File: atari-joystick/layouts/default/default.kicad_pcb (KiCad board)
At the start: 2 copper layers, 31.2 x 30 mm, 15 parts

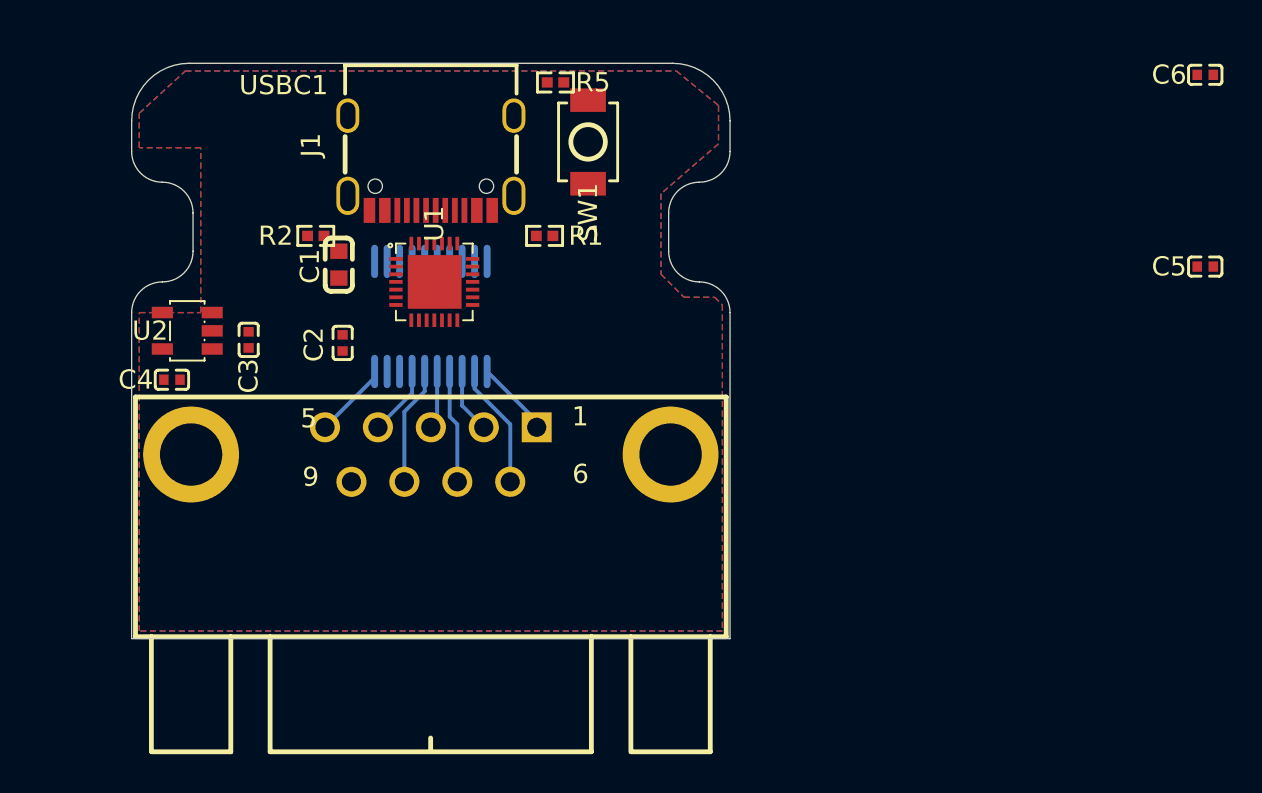
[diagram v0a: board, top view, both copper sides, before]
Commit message: atari-joystick: PCB レイアウト調整 (レベルシフタチャネル再割当含む)
配線取り回しを優先してレベルシフタの a1〜a7 ↔ joystick 信号の対応を再配置。
PCB 上の配置と配線も合わせて更新。

Co-Authored-By: Claude Opus 4.7 (1M context) <noreply@anthropic.com>
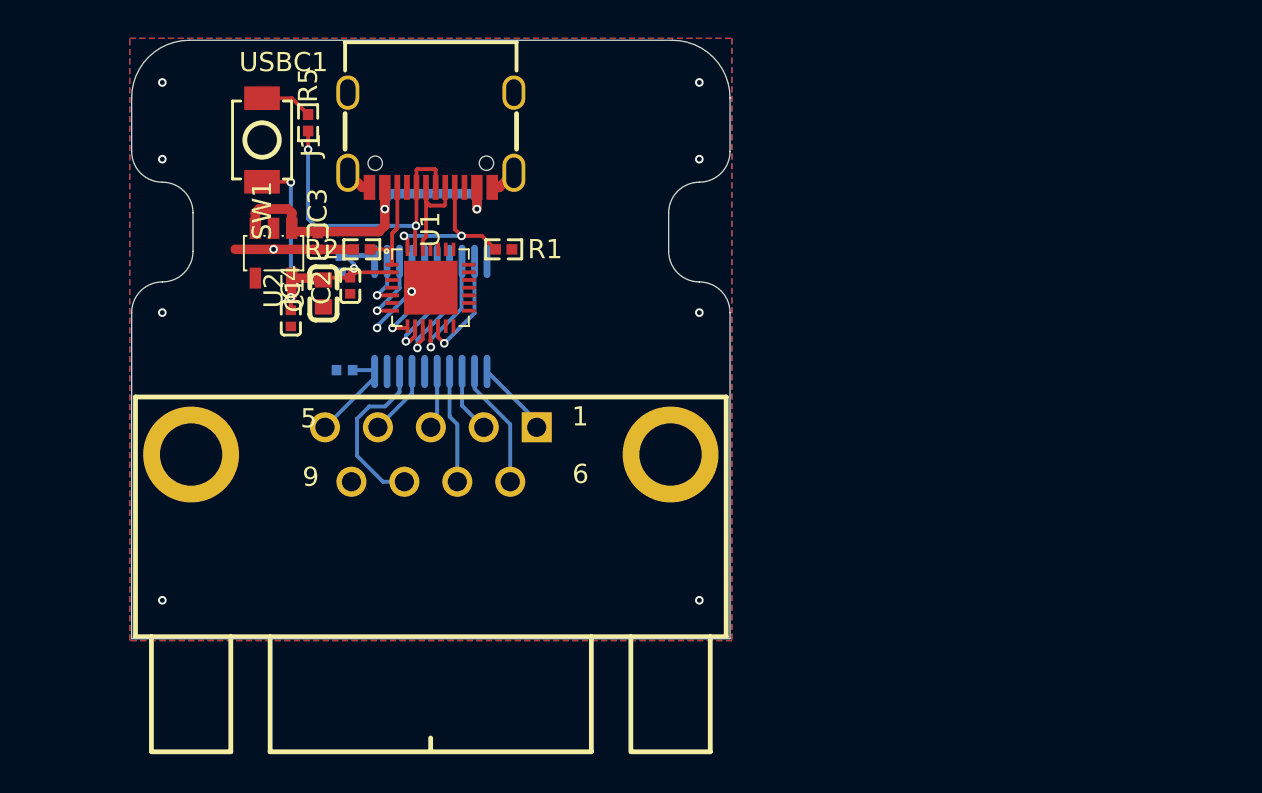
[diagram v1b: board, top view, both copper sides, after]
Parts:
- C5, C6: moved to B.Cu
- moved C6 47.4 mm to (105.5, 136.0), turned to 180 degrees
- moved C5 45.1 mm to (105.3, 130.5), turned to -90 degrees
- moved SW1 17.0 mm to (101.2, 124.0)
- moved R5 13.1 mm to (103.6, 123.1), turned to -90 degrees
- moved C4 6.98 mm to (102.7, 133.3), turned to -90 degrees
- moved C3 6.26 mm to (104.1, 129.3), turned to -90 degrees
- moved U2 6.05 mm to (101.8, 129.9), turned to 90 degrees
- moved C2 3.01 mm to (105.8, 131.6)
- moved R2 2.50 mm to (106.4, 129.7)
- moved R1 2.24 mm to (113.8, 129.7)
- moved C1 1.70 mm to (104.4, 132.0)
- moved USBC1 1.20 mm to (110.0, 124.0)
- moved U1 0.36 mm to (110.0, 131.7)
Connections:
- U3 pad 16: common -> b3
- U3 pad 18: b1 -> common
- U3 pad 2: GND -> COMMON_3V3
- U3 pad 4: COMMON_3V3 -> GND
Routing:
- net VDD33: track 0.00 -> 18.6 mm, vias 0 -> 3
- net VBUS: track 0.00 -> 18.0 mm, vias 0 -> 2
- net dp: track 0.00 -> 16.8 mm, vias 0 -> 2
- net GND: track 0.00 -> 13.3 mm, vias 0 -> 11
- net PC14_CC1_T1C3_T2C2_: track 0.00 -> 8.61 mm, vias 0 -> 2
- net DOWN_3V3: track 0.00 -> 6.47 mm, vias 0 -> 1
- net TRIGA_3V3: track 0.00 -> 6.25 mm, vias 0 -> 1
- net TRIGB_3V3: track 0.00 -> 5.96 mm, vias 0 -> 1
- net UP_3V3: track 0.00 -> 5.96 mm, vias 0 -> 1
- net PC15_CC2_T2C3_T1ET_: track 0.00 -> 5.61 mm
- net dn: track 0.00 -> 5.41 mm
- net LEFT_3V3: track 0.00 -> 4.95 mm, vias 0 -> 1
- net RIGHT_3V3: track 0.00 -> 3.83 mm, vias 0 -> 1
- net COMMON_3V3: track 0.00 -> 2.77 mm, vias 0 -> 1
- net terminal_b: track 0.00 -> 2.75 mm
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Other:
- board size 31.2 x 30 mm -> 31.2 x 31.2 mm

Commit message: atari-joystick: D-SUB シェルを GND に接続、フットプリント/PCB レイアウト調整
- joy.shell (D-SUB の固定金具) を vbus.lv に接続し、ケーブルシールド経由の
  リターンパスとシャーシ電位を 0V に固定
- D-SUB 9pin フットプリント (CONNFLY DS1037) を pcbnew で調整
- PCB レイアウトを配線取り回し優先で再調整

Co-Authored-By: Claude Opus 4.7 (1M context) <noreply@anthropic.com>
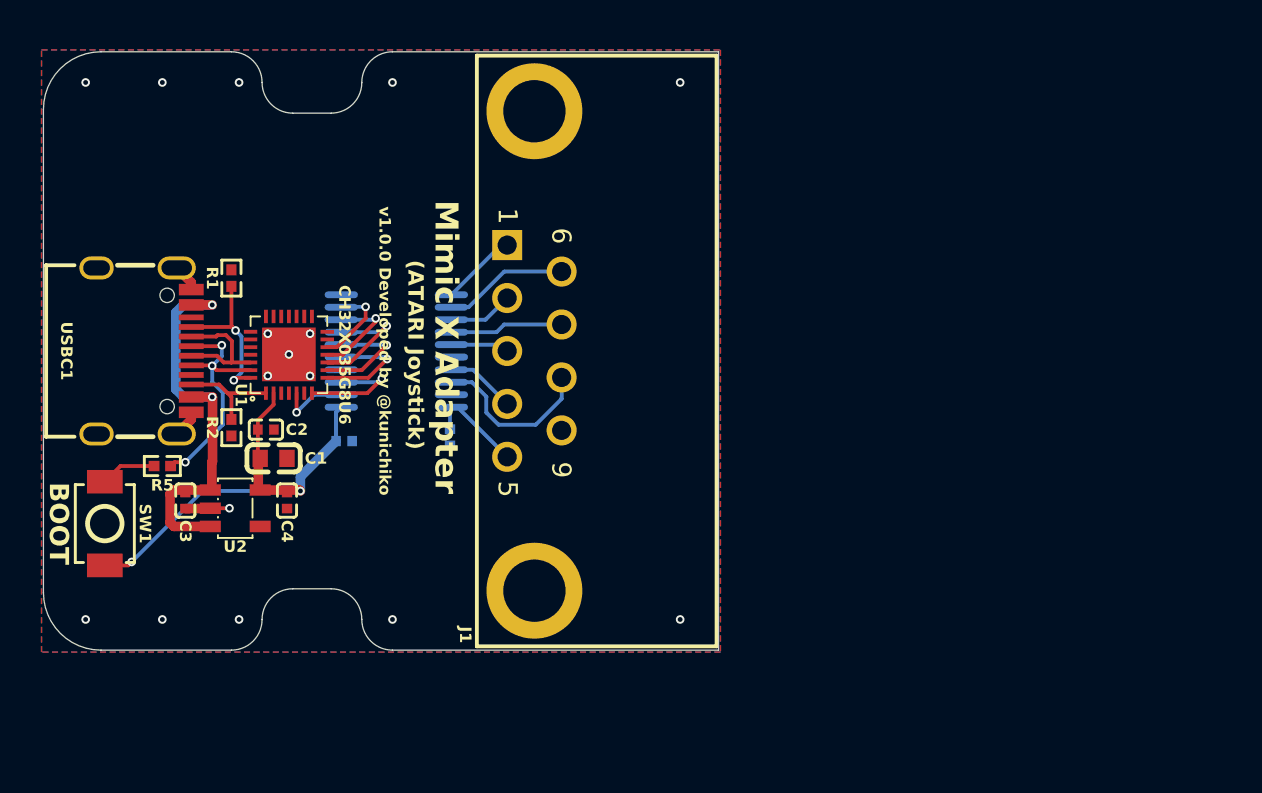
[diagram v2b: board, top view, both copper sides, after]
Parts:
- moved SW1 21.6 mm to (93.0, 144.0)
- moved R5 19.4 mm to (96.0, 141.0), turned to 0 degrees
- moved USBC1 18.6 mm to (95.0, 135.0), turned to -90 degrees
- moved C3 15.2 mm to (97.2, 142.8)
- moved R1 14.3 mm to (99.6, 131.2), turned to 90 degrees
- moved U2 13.4 mm to (99.8, 143.2), turned to 180 degrees
- moved R2 11.5 mm to (99.6, 139.0), turned to -90 degrees
- moved C4 9.50 mm to (102.5, 142.8)
- moved C5 9.22 mm to (105.5, 139.7), turned to 0 degrees
- moved C1 8.98 mm to (101.8, 140.6), turned to 0 degrees
- moved C2 8.70 mm to (101.4, 139.1), turned to 0 degrees
- moved U1 8.17 mm to (102.6, 135.2), turned to 0 degrees
- moved J1 7.64 mm to (115.4, 135.0), turned to 0 degrees
- moved C6 6.52 mm to (111.0, 139.5), turned to -90 degrees
- moved U3 2.55 mm to (108.2, 135.0), turned to 90 degrees
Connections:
- J1 pad 10: shell -> GND
- J1 pad 11: shell -> GND
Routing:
- net VDD33: track 18.6 -> 26.0 mm, vias 3 -> 2
- net GND: track 13.3 -> 8.27 mm, vias 11 -> 16
- net dp: track 16.8 -> 13.0 mm, vias 2 -> 3
- net VBUS: track 18.0 -> 21.2 mm
- net RIGHT_3V3: track 3.83 -> 6.15 mm
- net UP_3V3: track 5.96 -> 4.50 mm
- net dn: track 5.41 -> 6.64 mm
- net DOWN_3V3: track 6.47 -> 7.53 mm
- net LEFT_3V3: track 4.95 -> 5.96 mm
- net TRIGA_3V3: track 6.25 -> 5.28 mm
- net COMMON_3V3: track 2.77 -> 3.71 mm
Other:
- board size 31.2 x 31.2 mm -> 35.2 x 31.2 mm
- board text added: "(ATARI Joystick)"
- board text added: "BOOT"
- board text added: "CH32X035G8U6"
- board text added: "Mimic X Adapter"
- board text added: "v1.0.0 Developed by @kunichiko"

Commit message: atari-joystick: 電源 LED とフルカラー LED (WS2812B-2020) を追加
- LED1 (緑 0603, Hubei KT-0603G, C12624) + R3 (1kΩ): VDD33 常時点灯の
  電源インジケータ
- LED2 (Worldsemi WS2812B-2020, C965555): シリアル制御 RGB LED。
  MCU PB0 (QFN28 Pin 13) で DI を駆動、VDD33 共通電源
- parts/leds.ato に LedGreenKT0603 / LedRgbWs2812b ラッパーを追加

Co-Authored-By: Claude Opus 4.7 (1M context) <noreply@anthropic.com>
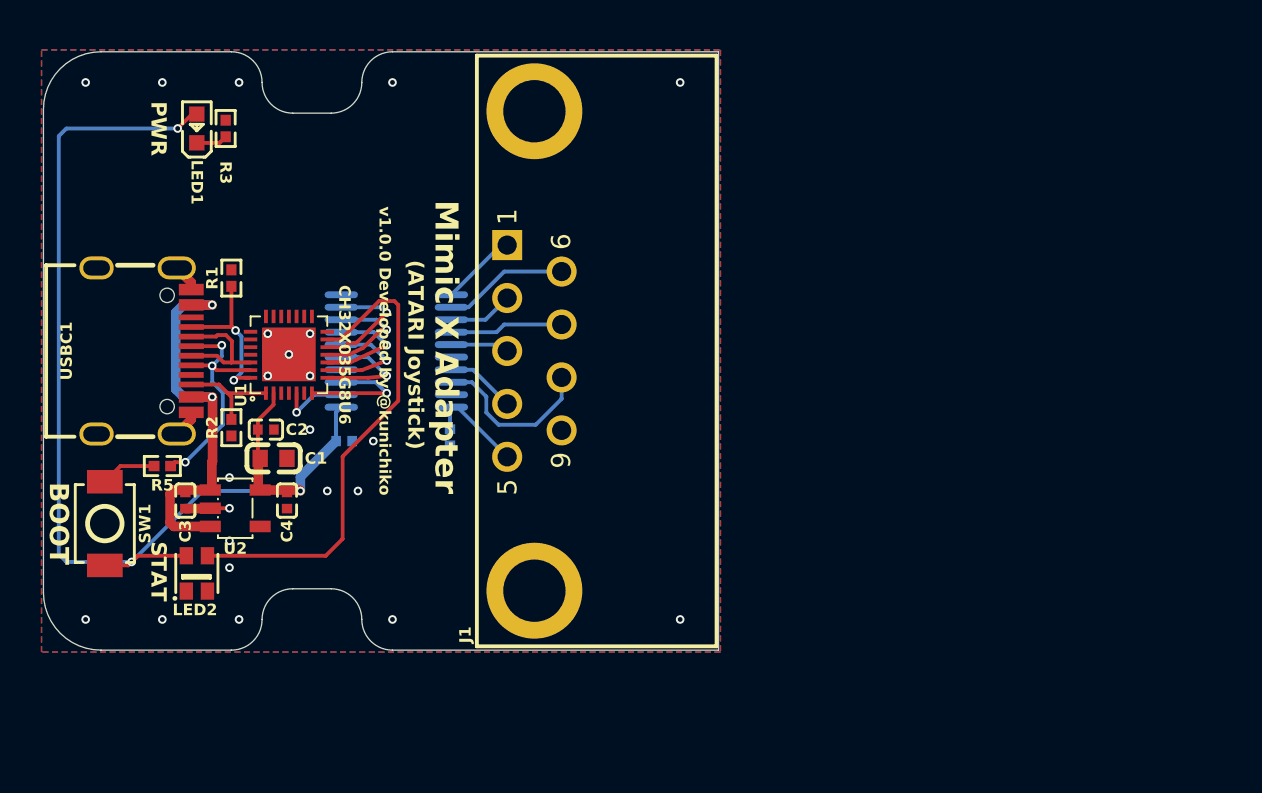
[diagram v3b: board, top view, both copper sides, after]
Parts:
- added LED1: , Hubei_KENTO_Elec_KT_0603G:LED0603-RD, F.Cu at (97.8, 123.4)
- added LED2: , Worldsemi_WS2812B_2020:LED-SMD_4P-L2.0-W2.0-TL_WS2812B-2020, F.Cu at (97.8, 146.6)
- added R3: 1kΩ ±1%, UNI_ROYAL_0402WGF1001TCE:R0402, F.Cu at (99.3, 123.4)
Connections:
- U1 pad 13: PB0 -> din
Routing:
- net din: track 0.00 -> 25.4 mm
- net VDD33: track 26.0 -> 36.7 mm, vias 2 -> 3
- net UP_3V3: track 4.50 -> 6.32 mm
- net cathode: track 0.00 -> 1.63 mm
- net TRIGA_3V3: track 5.28 -> 6.20 mm
- net GND: vias 16 -> 23
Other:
- board text added: "PWR"
- board text added: "STAT"

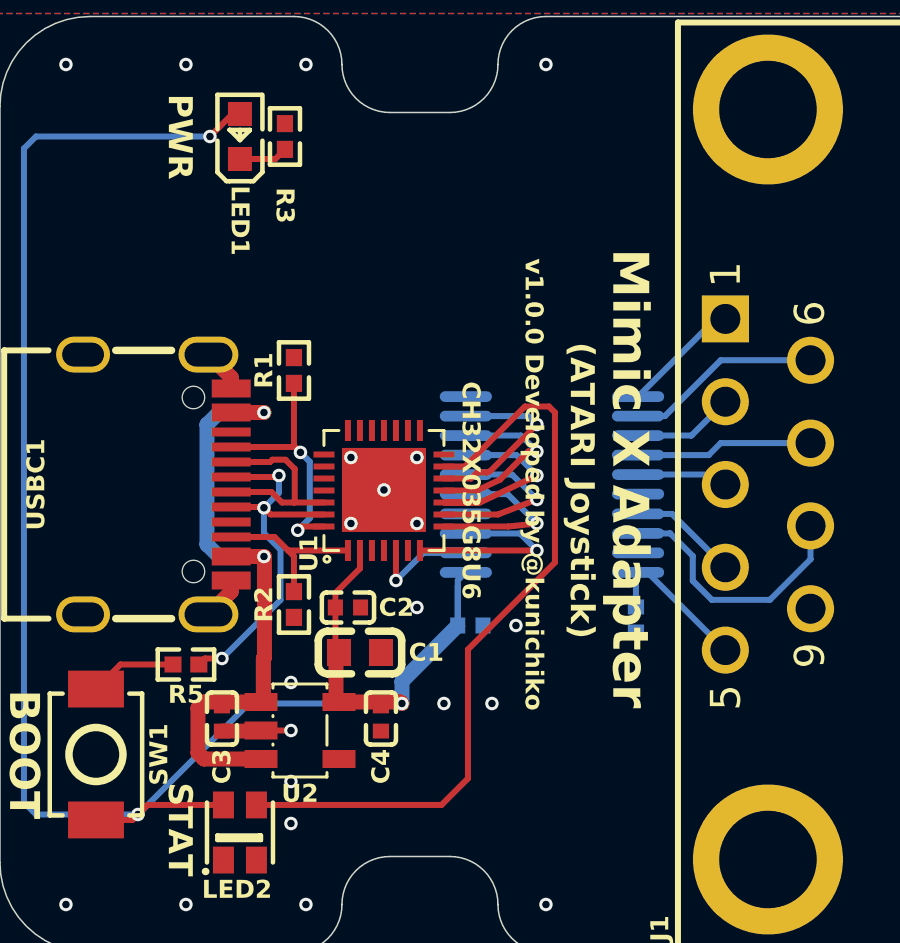
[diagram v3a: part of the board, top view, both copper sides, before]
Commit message: atari-joystick: WS2812B DI ラインに 470Ω 直列ダンピング抵抗 (R4) を追加
源端整合による反射制動と ESD 緩衝のために R4 (470Ω 0402) を MCU PB0 と
WS2812B DI の間に挿入。CH32X035 出力直近に寄せて配置する想定。

Co-Authored-By: Claude Opus 4.7 (1M context) <noreply@anthropic.com>
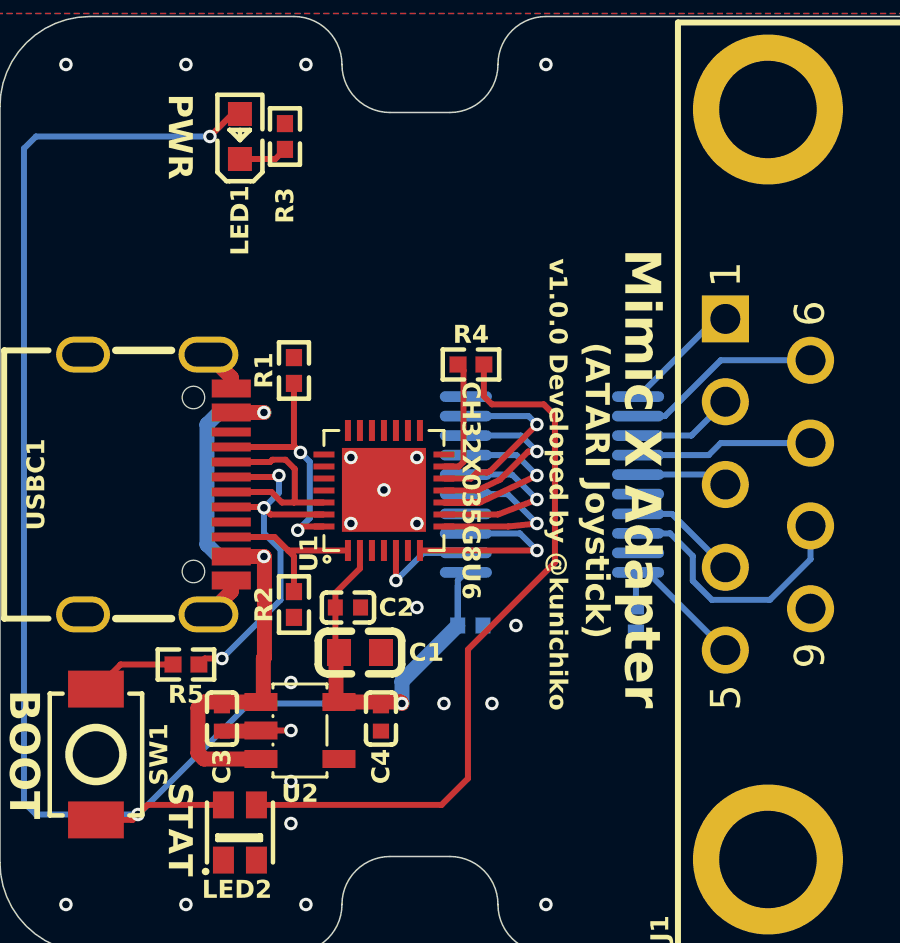
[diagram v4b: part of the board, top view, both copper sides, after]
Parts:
- added R4: 470Ω ±1%, UNI_ROYAL_0402WGF4700TCE:R0402, F.Cu at (105.5, 131.0)
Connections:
- U1 pad 13: din -> PB0
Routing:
- net PB0: track 0.00 -> 4.04 mm
- net din: track 25.4 -> 24.4 mm

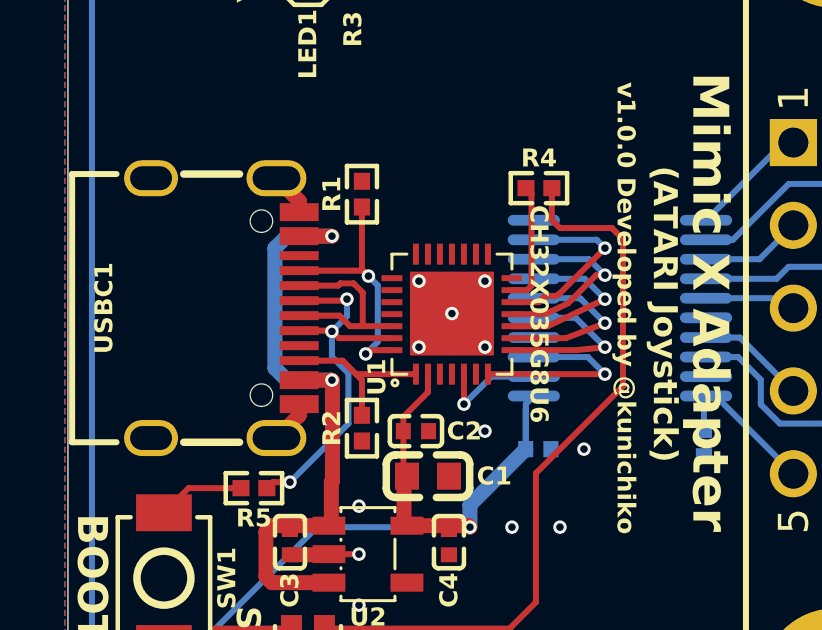
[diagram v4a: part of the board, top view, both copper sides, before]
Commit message: 両基板 v1.0.0: JLCPCB 発注用ファイル一式を確定
atari-joystick / x68000-keyboard ともに JLCPCB PCBA 発注用の Gerber ZIP /
BOM / CPL (positions) / designators を `layouts/default/production/` 配下に
v1.0.0 名義で固定。fabrication-toolkit プラグインの設定も合わせて記録する。

実発注に送付したファイル:
- atari-joystick/layouts/default/production/MimicX-Joystick-v1.0.0.zip 他
- x68000-keyboard/layouts/default/production/MimicX-Keyboard-v1.0.0.zip 他

Co-Authored-By: Claude Opus 4.7 (1M context) <noreply@anthropic.com>
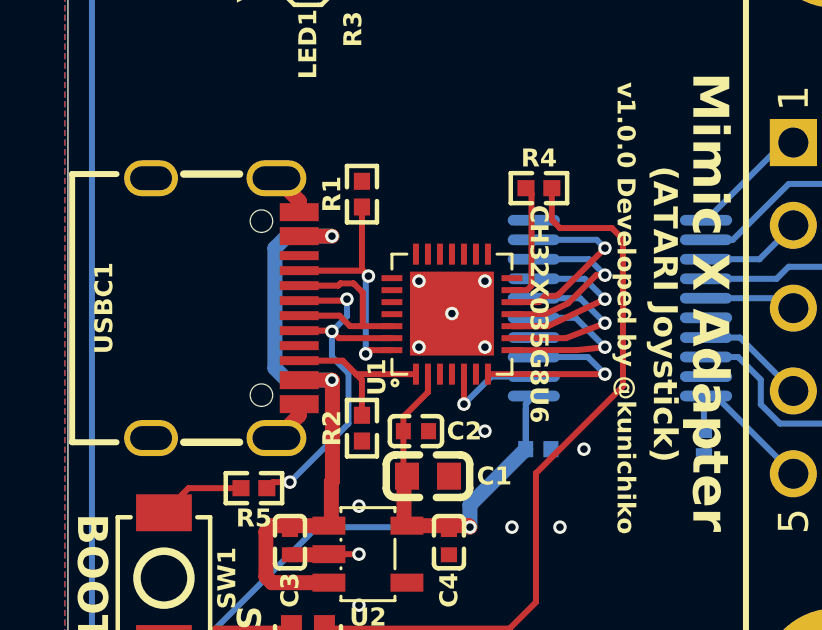
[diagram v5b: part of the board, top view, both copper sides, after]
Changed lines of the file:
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@@
 	)
 	(segment
-		(start 100.126 134.239659)
-		(end 99.817009 133.930668)
+		(start 99.7255 134.022177)
+		(end 99.7255 136.5255)
 		(width 0.2)
 		(layer "B.Cu")
@@
 	)
 	(segment
-		(start 99.7255 136.5255)
-		(end 100.126 136.125)
+		(start 99.817009 133.930668)
+		(end 99.7255 134.022177)
 		(width 0.2)
 		(layer "B.Cu")
-		(net 21)
-	)
-	(segment
-		(start 100.126 136.125)
-		(end 100.126 134.239659)
-		(width 0.2)
-		(layer "B.Cu")
